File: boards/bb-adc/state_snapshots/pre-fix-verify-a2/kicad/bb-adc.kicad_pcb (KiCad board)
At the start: 2 copper layers, 54.8 x 34.9 mm, 25 parts, among them J1 WJ500V-5.08-2P, J2 1x6P 2.54mm male header, U1 ADS8326IB, U2 ADR4520B, U3 OPA320

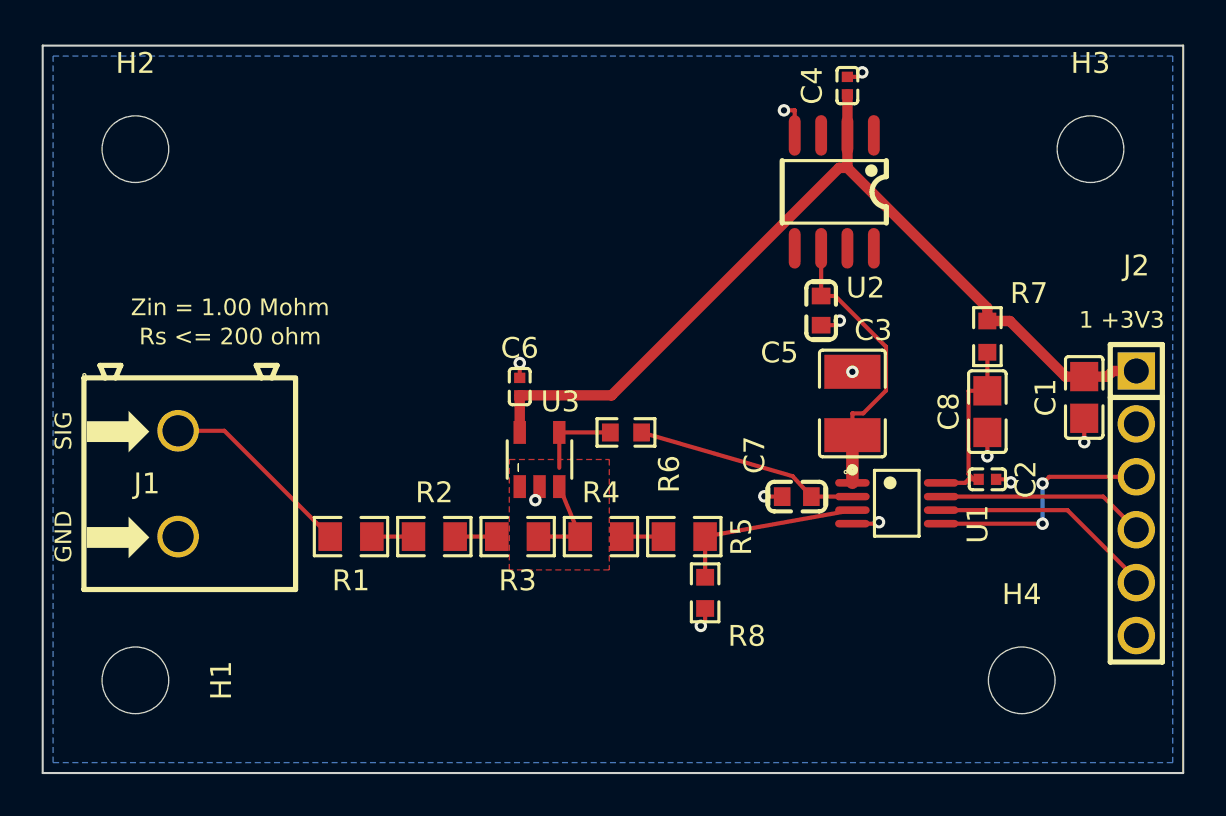
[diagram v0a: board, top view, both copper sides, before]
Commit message: ai-ee bb-adc: verify pass (J1 rotated, guard leakage paths cleared, silk complete)
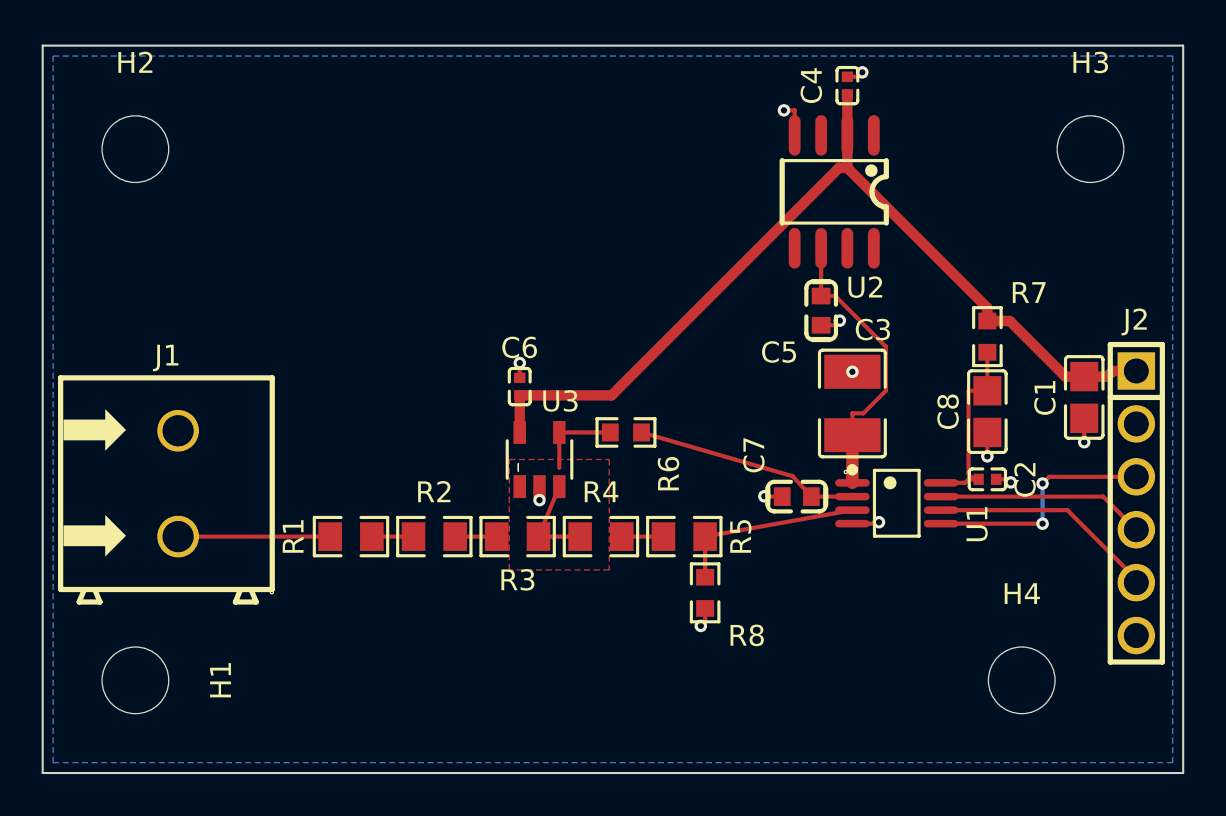
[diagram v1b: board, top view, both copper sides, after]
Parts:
- turned J1 to 90 degrees
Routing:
- net /AIN_RAW: track 9.40 -> 7.30 mm
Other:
- board text removed: "1 +3V3"
- board text removed: "GND"
- board text removed: "Rs <= 200 ohm"
- board text removed: "SIG"
- board text removed: "Zin = 1.00 Mohm"
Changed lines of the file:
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@@
 		(descr "2.54mm 1x6")
 		(property "Reference" "J2"
-			(at -11.4 0 0)
+			(at -8.795 0 0)
 			(layer "F.SilkS")
 			(effects
@@
 		(at 32.8 41.6)
 		(property "Reference" "R1"
-			(at 0 2.1135 0)
+			(at -2.7415 0 90)
 			(layer "F.SilkS")
 			(effects
@@
 		(locked yes)
 		(layer "F.Cu")
-		(at 24.5 39.06 -90)
+		(at 24.5 39.06 90)
 		(descr "WJ500V-5.08-2P")
 		(property "Reference" "J1"
-			(at 0 1.5 0)
+			(at 6.135 -0.5 0)
 			(layer "F.SilkS")
 			(effects
@@
 		)
 		(property "Value" "WJ500V-5.08-2P"
-			(at 0 4 270)
+			(at 0 4 90)
 			(layer "F.Fab")
 			(effects
@@
 		)
 		(property "Datasheet" ""
-			(at 0 0 270)
+			(at 0 0 90)
 			(layer "F.Fab")
 			(hide yes)
@@
 		)
 		(property "Description" ""
-			(at 0 0 270)
+			(at 0 0 90)
 			(layer "F.Fab")
 			(hide yes)
@@
 		)
 		(property "LCSC Part" "C8465"
-			(at 0 0 270)
+			(at 0 0 90)
 			(layer "F.Fab")
 			(hide yes)
@@
 		)
 		(property "LCSC" "C8465"
-			(at 0 0 270)
+			(at 0 0 90)
 			(layer "F.SilkS")
 			(hide yes)
@@
 		)
 		(property "Note" "ANALOG IN 0-5V: 1=SIG (Rs<=200ohm), 2=GND. LEFT edge, opening outward"
-			(at 0 0 270)
+			(at 0 0 90)
 			(layer "F.SilkS")
 			(hide yes)
@@
 		(duplicate_pad_numbers_are_jumpers no)
 		(fp_line
-			(start -5.08 4.52)
-			(end -5.08 -5.64)
+			(start 5.08 -5.64)
+			(end -5.05 -5.64)
 			(stroke
 				(width 0.25)
@@
 		)
 		(fp_line
-			(start 5.08 4.52)
-			(end -5.05 4.52)
+			(start -5.68 -4.75)
+			(end -5.68 -3.75)
 			(stroke
 				(width 0.25)
@@
 		)
 		(fp_line
-			(start 5.08 4.52)
-			(end 5.08 -5.64)
+			(start -5.08 -4.5)
+			(end -5.68 -4.75)
 			(stroke
 				(width 0.25)
@@
 		)
 		(fp_line
-			(start -5.68 3.75)
-			(end -5.08 3.5)
+			(start -5.68 -3.75)
+			(end -5.08 -4)
 			(stroke
 				(width 0.25)
@@
 		)
 		(fp_line
-			(start -5.08 3)
-			(end -5.68 2.75)
+			(start -5.68 2.75)
+			(end -5.68 3.75)
 			(stroke
 				(width 0.25)
@@
 		)
 		(fp_line
-			(start -5.68 2.75)
-			(end -5.68 3.75)
+			(start -5.08 3)
+			(end -5.68 2.75)
 			(stroke
 				(width 0.25)
@@
 		)
 		(fp_line
-			(start -5.68 -3.75)
-			(end -5.08 -4)
+			(start -5.68 3.75)
+			(end -5.08 3.5)
 			(stroke
 				(width 0.25)
@@
 		)
 		(fp_line
-			(start -5.08 -4.5)
-			(end -5.68 -4.75)
+			(start 5.08 4.52)
+			(end 5.08 -5.64)
 			(stroke
 				(width 0.25)
@@
 		)
 		(fp_line
-			(start -5.68 -4.75)
-			(end -5.68 -3.75)
+			(start 5.08 4.52)
+			(end -5.05 4.52)
 			(stroke
 				(width 0.25)
@@
 		)
 		(fp_line
-			(start 5.08 -5.64)
-			(end -5.05 -5.64)
+			(start -5.08 4.52)
+			(end -5.08 -5.64)
 			(stroke
 				(width 0.25)
@@
 		(fp_poly
 			(pts
-				(xy -2.999994 4.379989) (xy -1.999996 4.379989) (xy -1.999996 2.379993) (xy -1.499997 2.379993)
-				(xy -2.499995 1.379995) (xy -3.499993 2.379993) (xy -2.999994 2.379993) (xy -2.999994 4.379989)
+				(xy 2.080006 -5.499989) (xy 3.080004 -5.499989) (xy 3.080004 -3.499993) (xy 3.580003 -3.499993)
+				(xy 2.580005 -2.499995) (xy 1.580007 -3.499993) (xy 2.080006 -3.499993) (xy 2.080006 -5.499989)
 			)
 			(stroke
@@
 		(fp_poly
 			(pts
-				(xy 2.080006 4.379989) (xy 3.080004 4.379989) (xy 3.080004 2.379993) (xy 3.580003 2.379993) (xy 2.580005 1.379995)
-				(xy 1.580007 2.379993) (xy 2.080006 2.379993) (xy 2.080006 4.379989)
+				(xy -2.999994 -5.499989) (xy -1.999996 -5.499989) (xy -1.999996 -3.499993) (xy -1.499997 -3.499993)
+				(xy -2.499995 -2.499995) (xy -3.499993 -3.499993) (xy -2.999994 -3.499993) (xy -2.999994 -5.499989)
 			)
 			(stroke
@@
 		)
 		(fp_line
-			(start -5.21 4.5)
-			(end -5.21 -5.5)
+			(start 5.21 -5.5)
+			(end 5.21 4.5)
 			(stroke
 				(width 0.05)
@@
 		)
 		(fp_line
-			(start 5.21 4.5)
-			(end -5.21 4.5)
+			(start -5.21 -5.5)
+			(end 5.21 -5.5)
 			(stroke
 				(width 0.05)
@@
 		)
 		(fp_line
-			(start -5.21 -5.5)
-			(end 5.21 -5.5)
+			(start 5.21 4.5)
+			(end -5.21 4.5)
 			(stroke
 				(width 0.05)
@@
 		)
 		(fp_line
-			(start 5.21 -5.5)
-			(end 5.21 4.5)
+			(start -5.21 4.5)
+			(end -5.21 -5.5)
 			(stroke
 				(width 0.05)
@@
 		)
 		(fp_circle
-			(center -2.54 0)
-			(end -2.26 0)
+			(center 2.54 0)
+			(end 2.82 0)
 			(stroke
 				(width 0.55)
@@
 		)
 		(fp_circle
-			(center 2.54 0)
-			(end 2.82 0)
+			(center -2.54 0)
+			(end -2.26 0)
 			(stroke
 				(width 0.55)
@@
 		)
 		(fp_text user "${REFERENCE}"
-			(at 0 0 270)
+			(at 0 0 90)
 			(layer "F.Fab")
 			(effects
@@
 		)
 		(pad "1" thru_hole circle
-			(at -2.54 0 90)
+			(at -2.54 0 270)
 			(size 2 2)
 			(drill 1.5)
@@
 		)
 		(pad "2" thru_hole circle
-			(at 2.54 0 90)
+			(at 2.54 0 270)
 			(size 2 2)
 			(drill 1.5)
@@
 		(layer "Edge.Cuts")
 	)
-	(gr_text "Zin = 1.00 Mohm"
-		(at 27 30.6 0)
-		(layer "F.SilkS")
-		(effects
-			(font
-				(size 0.8 0.8)
-				(thickness 0.15)
-			)
-		)
-	)
-	(gr_text "Rs <= 200 ohm"
-		(at 27 32 0)
-		(layer "F.SilkS")
-		(effects
-			(font
-				(size 0.8 0.8)
-				(thickness 0.15)
-			)
-		)
-	)
-	(gr_text "1 +3V3"
-		(at 69.8 31.2 0)
-		(layer "F.SilkS")
-		(effects
-			(font
-				(size 0.8 0.8)
-				(thickness 0.15)
-			)
-		)
-	)
-	(gr_text "SIG"
-		(at 19 36.52 90)
-		(layer "F.SilkS")
-		(effects
-			(font
-				(size 0.8 0.8)
-				(thickness 0.15)
-			)
-		)
-	)
-	(gr_text "GND"
-		(at 19 41.6 90)
-		(layer "F.SilkS")
-		(effects
-			(font
-				(size 0.8 0.8)
-				(thickness 0.15)
-			)
-		)
-	)
 	(segment
 		(start 41.8 41.6)
@@
 	)
 	(segment
-		(start 43.8 41.6)
+		(start 41.8 41.6)
 		(end 42.8 39.2)
 		(width 0.2)
@@
 	)
 	(via
-		(at 40.9 33.2671)
+		(at 41.85 39.85)
 		(size 0.6)
 		(drill 0.3)
@@
 	)
 	(via
-		(at 68 37.0682)
+		(at 40.9 33.2671)
 		(size 0.6)
 		(drill 0.3)
@@
 	)
 	(via
-		(at 41.65 39.85)
+		(at 68 37.0682)
 		(size 0.6)
 		(drill 0.3)
@@
 	)
 	(segment
-		(start 24.5 36.52)
-		(end 26.72 36.52)
-		(width 0.2)
-		(layer "F.Cu")
-		(net "/AIN_RAW")
-	)
-	(segment
-		(start 26.72 36.52)
+		(start 24.5 41.6)
 		(end 31.8 41.6)
 		(width 0.2)
